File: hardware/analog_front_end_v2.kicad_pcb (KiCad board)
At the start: 4 copper layers, 146.1 x 45.5 mm, 105 parts, among them J1 Conn_Coaxial, J3 Conn_01x01_Socket, J4 Conn_01x01_Socket, U1 ADL5531, U10 MAX6002, U11 LP2985-5.0, U12 MAX2606, U13 PAT1220-C-0DB, U14 LP2985-5.0, U15 BFP540ESD, U16 BFP540ESD, U17 LP2985-3.3, U18 PAT1220-C-0DB, U19 PAT1220-C-0DB, U2 ADL5531, U20 PAT1220-C-0DB, U21 PAT1220-C-0DB, U22 MCP6286, U3 ADL5531, U4 ADL5531, U5 LP2985-1.8, U6 MCP33131, U7 PAT1220-C-0DB, U8 ADL5531, U9 PMOD 2x6 2.54mm pitch

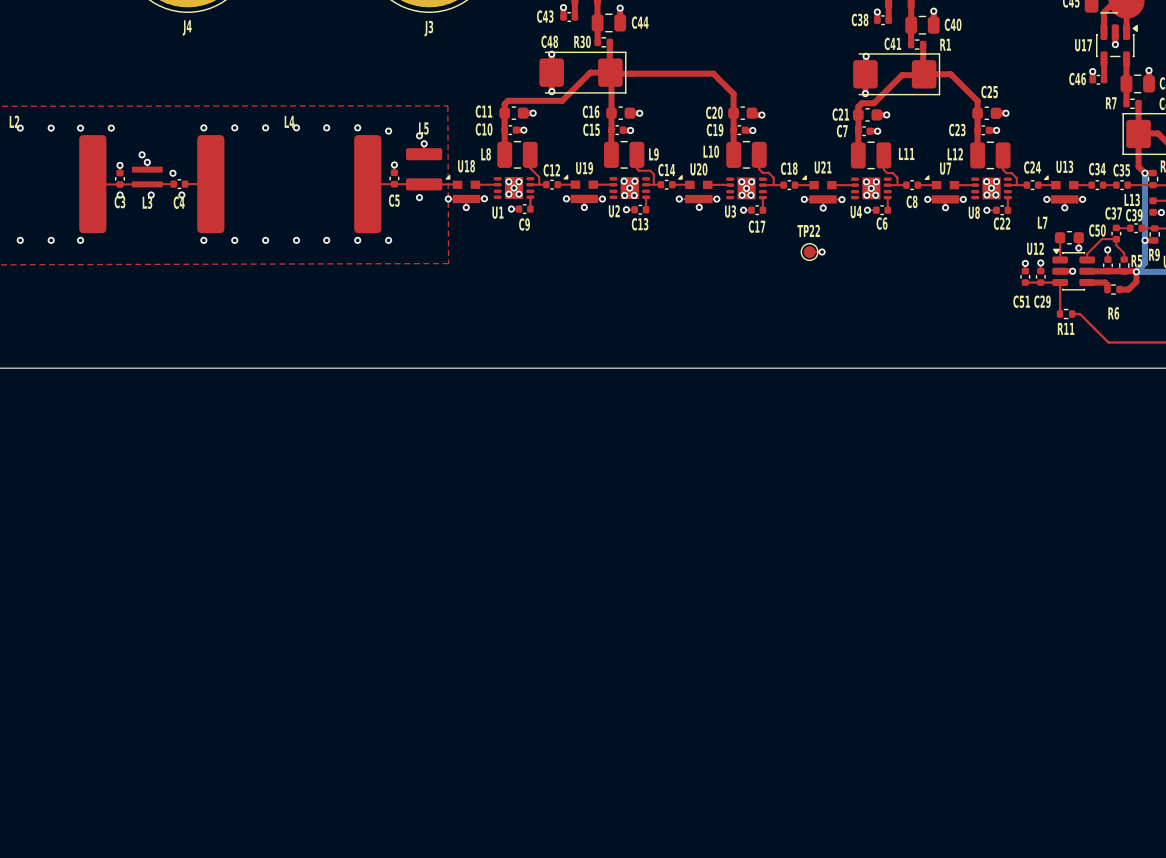
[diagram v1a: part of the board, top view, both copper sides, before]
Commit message: Update more passive MOC/Size/tolerances across the schematic
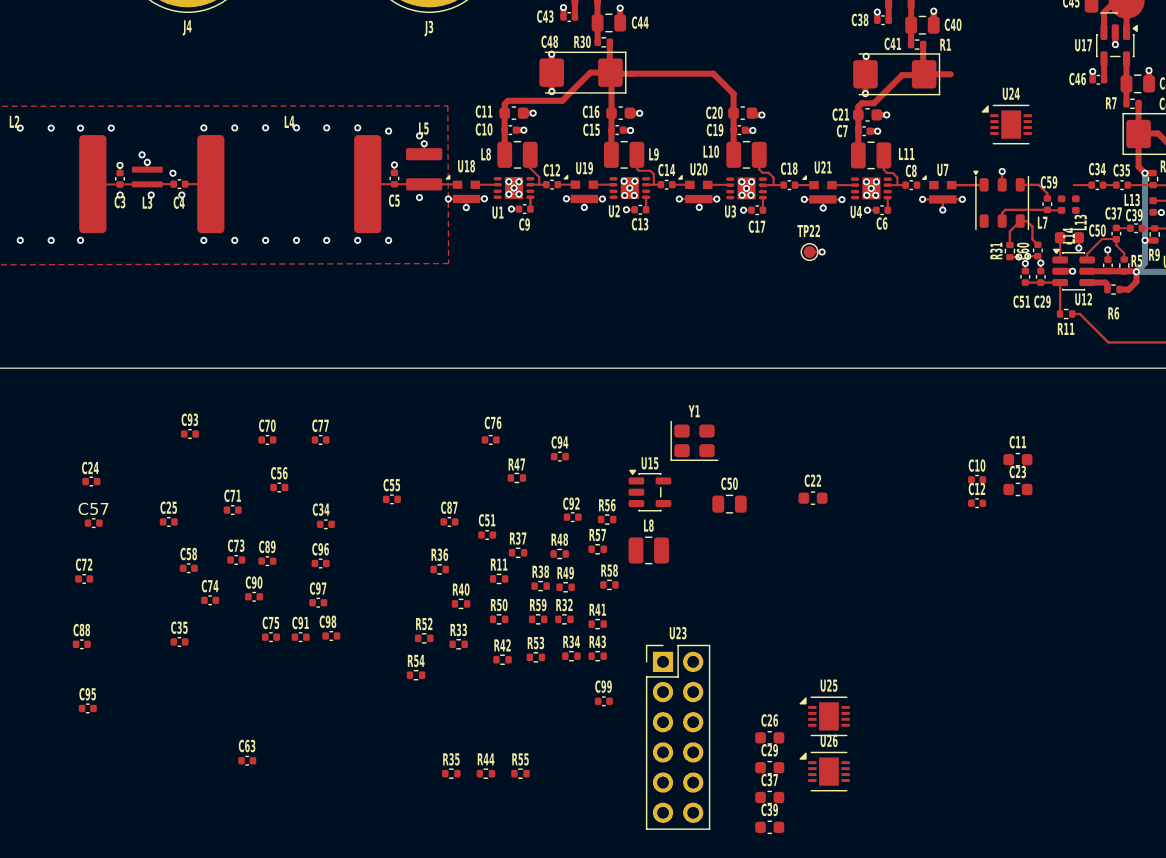
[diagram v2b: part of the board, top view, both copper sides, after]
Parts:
- removed L12: 470n, Inductor_SMD:L_1008_2520Metric
- removed U13: PAT1220-C-0DB, RF_Converter:RF_Attenuator_Susumu_PAT1220
- removed U8: ADL5531, TheEEView_Footprint_Lib:ADL5531
- added C10: 10n_25V, Capacitor_SMD:C_0402_1005Metric, F.Cu at (117.2, 65.4)
- added C11: 1u_16V, Capacitor_SMD:C_0603_1608Metric, F.Cu at (120.7, 63.7)
- added C12: 10n_25V, Capacitor_SMD:C_0402_1005Metric, F.Cu at (117.2, 67.3)
- added C26: 1u_16V, Capacitor_SMD:C_0603_1608Metric, F.Cu at (99.8, 87.1)
- added C29: 1u_16V, Capacitor_SMD:C_0603_1608Metric, F.Cu at (99.8, 89.6)
- added C34: 10n_25V, Capacitor_SMD:C_0402_1005Metric, F.Cu at (62.4, 69.1)
- added C35: 10n_25V, Capacitor_SMD:C_0402_1005Metric, F.Cu at (50.1, 79.0)
- added C37: 1u_16V, Capacitor_SMD:C_0603_1608Metric, F.Cu at (99.8, 92.1)
- added C39: 1u_16V, Capacitor_SMD:C_0603_1608Metric, F.Cu at (99.8, 94.6)
- added C50: 10u_16V, Capacitor_SMD:C_0805_2012Metric, F.Cu at (96.4, 67.4)
- added C51: 10n_25V, Capacitor_SMD:C_0402_1005Metric, F.Cu at (76.0, 70.0)
- added C55: 100n_25V, Capacitor_SMD:C_0402_1005Metric, F.Cu at (68.0, 67.0)
- added C56: 100n_25V, Capacitor_SMD:C_0402_1005Metric, F.Cu at (58.5, 66.0)
- added C57: 100n_25V, Capacitor_SMD:C_0402_1005Metric, F.Cu at (42.9, 69.0)
- added C58: 100n_25V, Capacitor_SMD:C_0402_1005Metric, F.Cu at (50.9, 72.8)
- added C59: 27p, Capacitor_SMD:C_0402_1005Metric, F.Cu at (123.2, 42.1)
- added C60: 1n, Capacitor_SMD:C_0402_1005Metric, F.Cu at (122.3, 46.0)
- added C63: 100p, Capacitor_SMD:C_0402_1005Metric, F.Cu at (55.8, 89.0)
- added C70: 390p, Capacitor_SMD:C_0402_1005Metric, F.Cu at (57.5, 62.0)
- added C71: 130p, Capacitor_SMD:C_0402_1005Metric, F.Cu at (54.6, 67.9)
- added C72: 130p, Capacitor_SMD:C_0402_1005Metric, F.Cu at (42.1, 73.7)
- added C73: 910p, Capacitor_SMD:C_0402_1005Metric, F.Cu at (54.9, 72.1)
- added C74: 56p, Capacitor_SMD:C_0402_1005Metric, F.Cu at (52.7, 75.5)
- added C75: 56p, Capacitor_SMD:C_0402_1005Metric, F.Cu at (57.8, 78.6)
- added C76: 1n8, Capacitor_SMD:C_0402_1005Metric, F.Cu at (76.3, 62.0)
- added C77: 1n8, Capacitor_SMD:C_0402_1005Metric, F.Cu at (62.0, 62.0)
- added C87: 100n_25V, Capacitor_SMD:C_0402_1005Metric, F.Cu at (72.8, 68.9)
- added C88: 100n_25V, Capacitor_SMD:C_0402_1005Metric, F.Cu at (41.9, 79.2)
- added C89: 1n5, Capacitor_SMD:C_0402_1005Metric, F.Cu at (57.5, 72.2)
- added C90: 15n, Capacitor_SMD:C_0402_1005Metric, F.Cu at (56.4, 75.2)
- added C91: 150p, Capacitor_SMD:C_0402_1005Metric, F.Cu at (60.3, 78.6)
- added C92: 100n_25V, Capacitor_SMD:C_0402_1005Metric, F.Cu at (83.2, 68.5)
- added C93: 100n_25V, Capacitor_SMD:C_0402_1005Metric, F.Cu at (51.0, 61.5)
- added C94: 100n_25V, Capacitor_SMD:C_0402_1005Metric, F.Cu at (82.1, 63.4)
- added C95: 100n_25V, Capacitor_SMD:C_0402_1005Metric, F.Cu at (42.4, 84.6)
- added C96: 100n_25V, Capacitor_SMD:C_0402_1005Metric, F.Cu at (62.0, 72.4)
- added C97: 100n_25V, Capacitor_SMD:C_0402_1005Metric, F.Cu at (61.8, 75.7)
- added C98: 100n_25V, Capacitor_SMD:C_0402_1005Metric, F.Cu at (62.9, 78.5)
- added C99: 100n_25V, Capacitor_SMD:C_0402_1005Metric, F.Cu at (85.8, 84.0)
- added L13: 18n, Inductor_SMD:L_0402_1005Metric, F.Cu at (124.3, 42.2)
- added L14: 18n, Inductor_SMD:L_0402_1005Metric, F.Cu at (125.5, 42.2)
- added L8: 470n, Inductor_SMD:L_1008_2520Metric, F.Cu at (89.6, 71.3)
- added R11: 5.1k, Resistor_SMD:R_0402_1005Metric, F.Cu at (77.0, 73.7)
- added R31: 3R0, Resistor_SMD:R_0402_1005Metric, F.Cu at (120.0, 46.1)
- added R32: 162R, Resistor_SMD:R_0402_1005Metric, F.Cu at (82.5, 77.1)
- added R33: 330R, Resistor_SMD:R_0402_1005Metric, F.Cu at (73.6, 79.2)
- added R34: 330R, Resistor_SMD:R_0402_1005Metric, F.Cu at (83.1, 80.2)
- added R35: 1k00, Resistor_SMD:R_0402_1005Metric, F.Cu at (73.0, 90.1)
- added R36: 1k00, Resistor_SMD:R_0402_1005Metric, F.Cu at (72.0, 72.9)
- added R37: 1k00, Resistor_SMD:R_0402_1005Metric, F.Cu at (78.6, 71.5)
- added R38: 1k00, Resistor_SMD:R_0402_1005Metric, F.Cu at (80.5, 74.3)
- added R40: 4k02, Resistor_SMD:R_0402_1005Metric, F.Cu at (73.8, 75.8)
- added R41: 1k00, Resistor_SMD:R_0402_1005Metric, F.Cu at (85.3, 77.5)
- added R42: 1k00, Resistor_SMD:R_0402_1005Metric, F.Cu at (77.3, 80.5)
- added R43: 1k00, Resistor_SMD:R_0402_1005Metric, F.Cu at (85.3, 80.2)
- added R44: 1k00, Resistor_SMD:R_0402_1005Metric, F.Cu at (75.9, 90.1)
- added R47: 22R0, Resistor_SMD:R_0402_1005Metric, F.Cu at (78.5, 65.2)
- added R48: 22R0, Resistor_SMD:R_0402_1005Metric, F.Cu at (82.1, 71.6)
- added R49: 20k0, Resistor_SMD:R_0402_1005Metric, F.Cu at (82.6, 74.4)
- added R50: 20k0, Resistor_SMD:R_0402_1005Metric, F.Cu at (77.0, 77.1)
- added R52: 50R, Resistor_SMD:R_0402_1005Metric, F.Cu at (70.7, 78.7)
- added R53: 33R, Resistor_SMD:R_0402_1005Metric, F.Cu at (80.1, 80.3)
- added R54: 1k37, Resistor_SMD:R_0402_1005Metric, F.Cu at (70.0, 81.8)
- added R55: 6k19, Resistor_SMD:R_0402_1005Metric, F.Cu at (78.8, 90.1)
- added R56: 4k02, Resistor_SMD:R_0402_1005Metric, F.Cu at (86.1, 68.7)
- added R57: 4k02, Resistor_SMD:R_0402_1005Metric, F.Cu at (85.3, 71.2)
- added R58: 4k02, Resistor_SMD:R_0402_1005Metric, F.Cu at (86.3, 74.2)
- added R59: 50R, Resistor_SMD:R_0402_1005Metric, F.Cu at (80.3, 77.1)
- added T1: WBC1-1TL 1:1, fm-radio-footprint-lib:WBC1-1TLC, F.Cu at (119.3, 42.0)
- added U15: LP2985-5.0, Package_TO_SOT_SMD:SOT-23-5, F.Cu at (89.7, 66.4)
- added U23: PMOD 2x6 2.54mm pitch, Connector_PinHeader_2.54mm:PinHeader_2x06_P2.54mm_Vertical, F.Cu at (90.8, 80.7)
- added U24: LT5560, Package_DFN_QFN:DFN-8-1EP_3x3mm_P0.5mm_EP1.66x2.38mm, F.Cu at (120.1, 35.5)
- added U25: LTC6362, Package_DFN_QFN:DFN-8-1EP_3x3mm_P0.5mm_EP1.66x2.38mm, F.Cu at (104.8, 85.3)
- added U26: LTC6362, Package_DFN_QFN:DFN-8-1EP_3x3mm_P0.5mm_EP1.66x2.38mm, F.Cu at (104.8, 89.9)
- added Y1: 12.8MHz TCXO, Oscillator:Oscillator_SMD_Abracon_ASE-4Pin_3.2x2.5mm, F.Cu at (93.5, 62.1)
- C2, C4: value 5p1_50V -> 4p8_50V
- C22: value 1n_50V -> 1u_16V; footprint Capacitor_SMD:C_0402_1005Metric -> Capacitor_SMD:C_0603_1608Metric
- C23: value 10n_25V -> 1u_16V; footprint Capacitor_SMD:C_0402_1005Metric -> Capacitor_SMD:C_0603_1608Metric
- C24: value 10n_25V -> 1n_50V
- C25: value 1u_16V -> 1n_50V; footprint Capacitor_SMD:C_0603_1608Metric -> Capacitor_SMD:C_0402_1005Metric
- C3: value 240p_50V -> 220p_50V
- moved C24 83.1 mm to (42.7, 65.5)
- moved C25 77.0 mm to (49.2, 68.9)
- moved C23 30.4 mm to (120.7, 66.2)
- moved C22 29.0 mm to (103.4, 66.9), turned to 0 degrees
- moved U7 0.23 mm to (114.3, 41.1)
- moved C8 0.07 mm to (111.7, 40.5)
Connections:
- C19 pad 1: 5V_LNA1 -> 5V_LNA2
- C20 pad 1: 5V_LNA1 -> 5V_LNA2
- C22 pad 1: Net-(U8-CLIN) -> 3V3
- C23 pad 1: 5V_LNA2 -> 5V_MIX
- C24 pad 1: Net-(U8-RFOUT) -> 5V_MIX
- C24 pad 2: Net-(C24-Pad2) -> GND
- C25 pad 1: 5V_LNA2 -> Net-(U24-OUT+)
- C25 pad 2: GND -> Net-(U24-OUT-)
- L10 pad 2: 5V_LNA1 -> 5V_LNA2
- R2 pad 2: Net-(C26-Pad1) -> ADC_VCM
- U22 pad 3: Net-(U15-C) -> VCM_DIV
- U6 pad 3: Net-(U6-AIN+) -> ADC_AIN_P
- U6 pad 4: GND -> ADC_AIN_N
- U9 pad 10: PWM_TUNE -> unconnected-(U9-Pad10)
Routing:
- net 5V_LNA2: track 26.1 -> 17.9 mm
- net Net-(T1-SB): track 0.00 -> 5.80 mm
- net MIX_BIAS: track 0.00 -> 5.31 mm
- net Net-(U8-RFOUT): track 5.03 -> 0.00 mm
- net GND: track 84.2 -> 80.5 mm, vias 167 -> 159
- net Net-(T1-SA): track 0.00 -> 3.00 mm
- net Net-(C8-Pad2): track 1.58 -> 0.00 mm
- net Net-(C24-Pad2): track 1.48 -> 0.00 mm
- net Net-(U8-CLIN): track 1.07 -> 0.00 mm
- net ADC_AIN_N: track 0.00 -> 1.03 mm
- net Net-(T1-AA): track 1.75 -> 2.74 mm

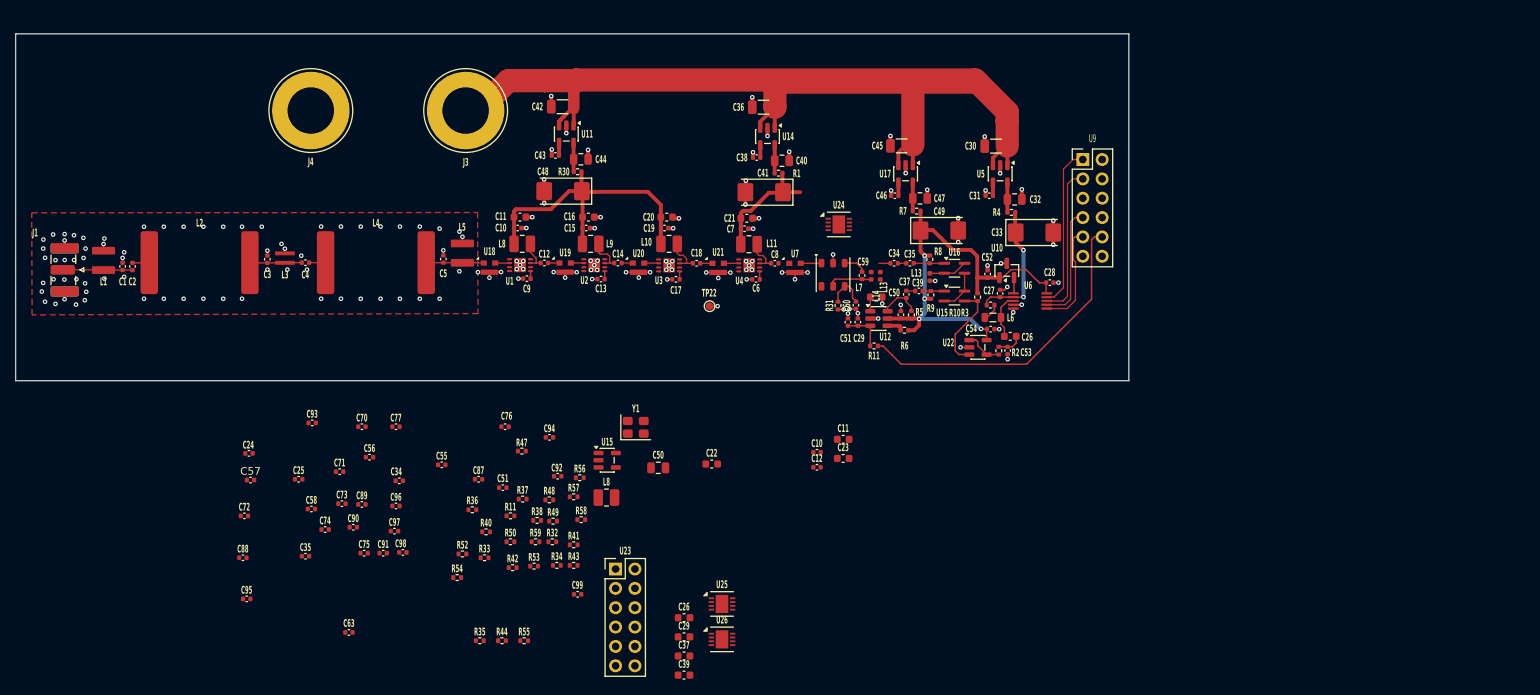
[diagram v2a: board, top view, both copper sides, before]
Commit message: More routing and move frontend inductor to be perpendicular
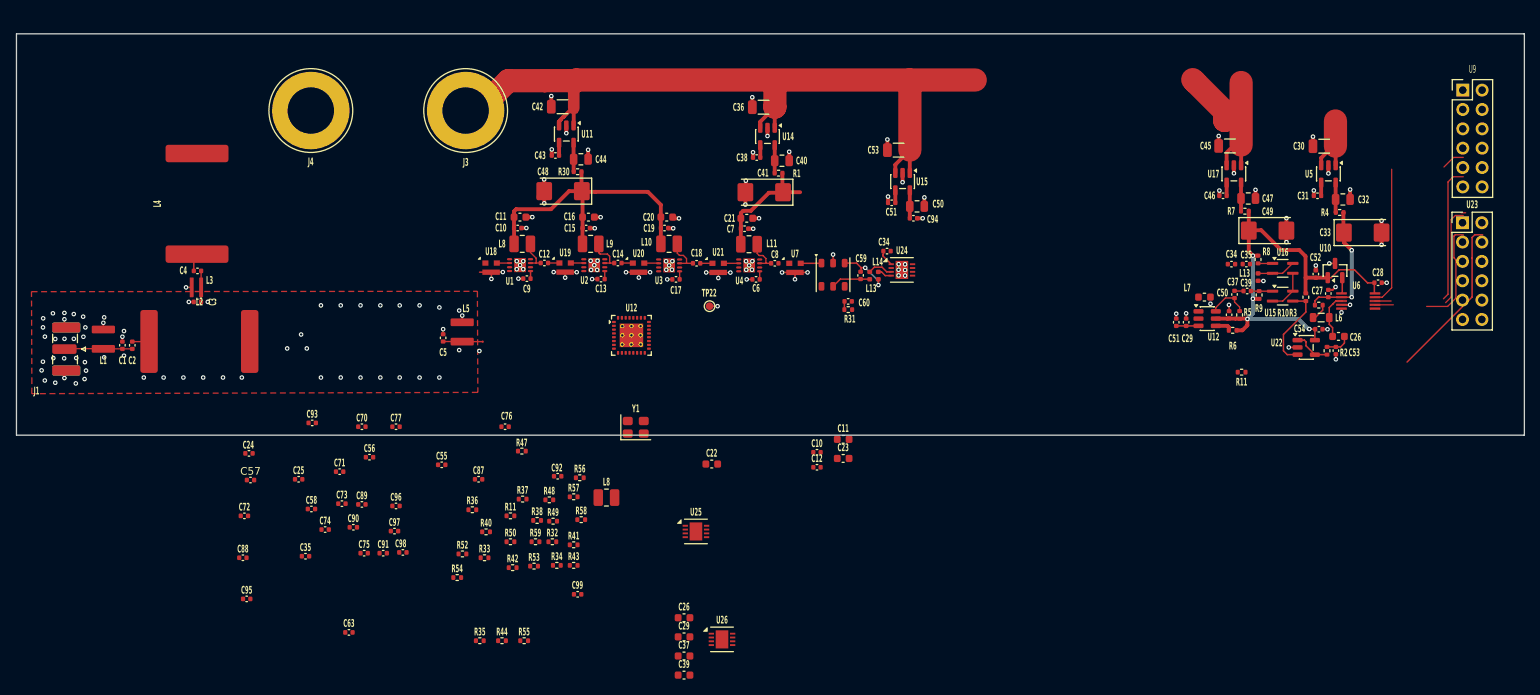
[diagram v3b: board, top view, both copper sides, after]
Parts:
- added C53: 10u_50V, Capacitor_SMD:C_1206_3216Metric, F.Cu at (128.0, 25.7)
- added U12: ADF4531, fm-radio-footprint-lib:ADF4351_LFCSP-32_5x5mm_P0.5mm_EP3.1x3.1mm, F.Cu at (92.9, 50.0)
- moved U23 120.1 mm to (202.0, 35.2)
- moved C34 70.8 mm to (126.4, 39.0)
- moved C51 63.3 mm to (127.0, 32.6)
- moved C94 55.8 mm to (129.9, 34.6)
- moved U15 53.3 mm to (128.5, 29.8), turned to -90 degrees
- moved U9 50.7 mm to (202.0, 17.8)
- moved R11 48.4 mm to (173.0, 54.8)
- moved C50 48.3 mm to (130.4, 33.1), turned to 180 degrees
- moved C34 44.3 mm to (171.6, 40.7)
- moved C35 44.2 mm to (173.6, 40.6)
- moved C51 43.1 mm to (164.4, 48.3)
- moved C29 43.1 mm to (165.7, 48.3)
- moved C26 43.1 mm to (185.7, 50.1)
- moved C30 43.1 mm to (183.8, 25.2)
- moved C31 43.1 mm to (182.9, 31.7)
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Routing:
- net PWM_TUNE: track 41.9 -> 21.4 mm
- net VIN: track 145.4 -> 134.8 mm
- net Net-(T1-SA): track 3.00 -> 7.26 mm, vias 0 -> 2
- net MIX_BIAS: track 5.31 -> 1.19 mm
- net 5V_MIX: track 0.00 -> 3.67 mm
- net Net-(U24-IN+): track 0.00 -> 3.33 mm
- net Net-(C3-Pad1): track 6.85 -> 4.12 mm
- net Net-(U12-TUNE): track 5.58 -> 2.93 mm
- net Net-(C5-Pad1): track 7.48 -> 5.23 mm
- net Net-(U24-LO-): track 0.00 -> 2.17 mm
- net GND: track 80.5 -> 82.6 mm
- net Net-(U16-B): track 3.94 -> 1.81 mm
- net Net-(U24-IN-): track 0.00 -> 1.90 mm
- net Net-(U12-IND): track 1.79 -> 0.00 mm
- net Net-(U15-BP): track 0.00 -> 1.64 mm
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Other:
- board size 146.1 x 45.5 mm -> 197.9 x 52.7 mm

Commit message: Updated schematics/PCB files
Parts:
- removed C94: 100n_25V, Capacitor_SMD:C_0402_1005Metric
- added C60: 1n_50V, Capacitor_SMD:C_0402_1005Metric, F.Cu at (119.6, 55.5)
- added C61: 100n_25V, Capacitor_SMD:C_0402_1005Metric, F.Cu at (70.6, 51.8)
- added C62: 100n_25V, Capacitor_SMD:C_0402_1005Metric, F.Cu at (68.9, 46.0)
- added C64: 100n_25V, Capacitor_SMD:C_0402_1005Metric, F.Cu at (68.9, 44.9)
- added C65: 47u_16V, Capacitor_Tantalum_SMD:CP_EIA-6032-15_Kemet-U, F.Cu at (68.6, 27.3)
- added R8: 0R, Resistor_SMD:R_0402_1005Metric, F.Cu at (70.5, 24.7)
- C63: value 100p -> 100p_250V
- C90: footprint Capacitor_SMD:C_0402_1005Metric -> Capacitor_SMD:C_0603_1608Metric
- R31: footprint Resistor_SMD:R_0402_1005Metric -> Resistor_SMD:R_0805_2012Metric
- moved U17 93.6 mm to (78.8, 19.5)
- moved C45 93.6 mm to (78.3, 15.8)
- moved C46 93.6 mm to (77.4, 22.4)
- moved C47 93.6 mm to (80.7, 22.7)
- moved R7 93.6 mm to (80.3, 24.4)
- moved C49 93.6 mm to (83.3, 26.9)
- moved U7 67.4 mm to (47.1, 45.7)
- moved C60 67.2 mm to (54.3, 50.3)
- moved T1 67.2 mm to (52.3, 46.6)
- moved C8 67.2 mm to (44.6, 42.9), turned to -90 degrees
- moved R31 66.8 mm to (54.7, 52.1)
- moved C6 66.4 mm to (42.8, 44.6)
- moved U21 66.4 mm to (37.9, 43.1)
- moved U4 66.4 mm to (41.9, 42.7)
- moved C18 65.7 mm to (35.8, 40.9), turned to -90 degrees
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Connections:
- C50 pad 2: 5V_MIX -> Net-(U15-VOUT)
- U15 pad 5: 5V_MIX -> Net-(U15-VOUT)
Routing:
- net VIN: track 134.8 -> 90.1 mm
- net 5V_LNA2: track 17.9 -> 53.8 mm
- net Net-(C3-Pad1): track 4.12 -> 30.0 mm
- net GND: track 82.6 -> 99.8 mm, vias 159 -> 155
- net 3V3: track 59.2 -> 70.8 mm
- net Net-(C5-Pad1): track 5.23 -> 11.8 mm
- net Net-(Y1-OUT): track 0.00 -> 5.58 mm
- net Net-(T1-SB): track 5.25 -> 1.18 mm
- net Net-(U15-VOUT): track 0.00 -> 3.67 mm
- net Net-(C8-Pad2): track 0.00 -> 2.91 mm
- net MIX_BIAS: track 1.19 -> 3.98 mm
- net Net-(T1-SA): track 7.26 -> 4.85 mm
- net Net-(U1-RFIN): track 1.54 -> 3.90 mm
- net PLL_REF: track 0.00 -> 2.16 mm
- net 5V_LNA1: track 41.7 -> 43.3 mm
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- removed copper zone on F.Cu, net GND
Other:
- board size 197.9 x 52.7 mm -> 197.9 x 55.1 mm
